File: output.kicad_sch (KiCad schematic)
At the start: 108 parts, among them J10 DB301V-3.5-3P-GN, J11 DB301V-3.5-3P-GN, J12 DB301V-3.5-3P-GN, J13 DB301V-3.5-3P-GN, J14 DB301V-3.5-3P-GN, J15 DB301V-3.5-3P-GN, J16 DB301V-3.5-3P-GN, J17 DB301V-3.5-3P-GN, J18 DB301V-3.5-3P-GN, J19 DB301V-3.5-3P-GN, J20 DB301V-3.5-3P-GN, J21 DB301V-3.5-3P-GN, J22 DB301V-3.5-3P-GN, J23 DB301V-3.5-3P-GN, J24 DB301V-3.5-3P-GN, J25 DB301V-3.5-3P-GN, J26 DB301V-3.5-3P-GN, J27 DB301V-3.5-3P-GN, J28 DB301V-3.5-3P-GN, J29 DB301V-3.5-3P-GN, J30 DB301V-3.5-3P-GN, J31 DB301V-3.5-3P-GN, J32 DB301V-3.5-3P-GN, J33 DB301V-3.5-3P-GN, J34 DB301V-3.5-3P-GN, J35 DB301V-3.5-3P-GN, J36 DB301V-3.5-3P-GN, J5 DB301V-3.5-3P-GN, J6 DB301V-3.5-3P-GN, J7 DB301V-3.5-3P-GN, J8 DB301V-3.5-3P-GN, J9 DB301V-3.5-3P-GN, U5 SN74LVC8T245PWR, U6 SN74LVC8T245PWR, U7 SN74LVC8T245PWR, U8 SN74LVC8T245PWR

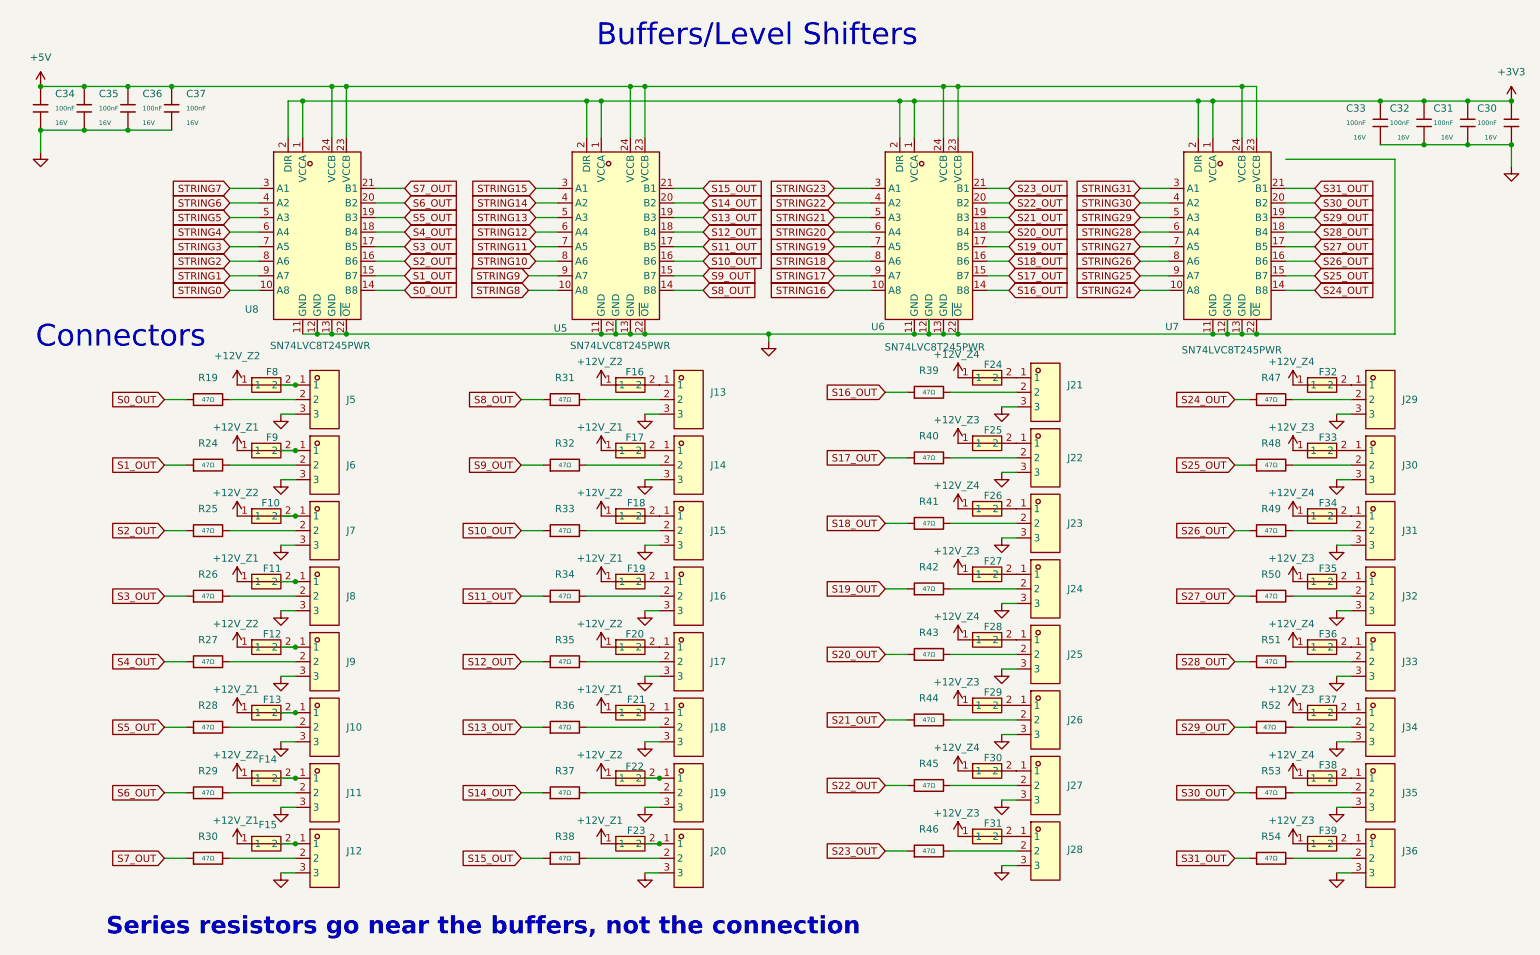
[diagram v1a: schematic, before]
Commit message: Zone silkscreen, 30V port PTCs, string renumbering
- Port PTCs: LUTE 1812L300/30GR (C48985875) imported via jlcimport, pins
  redrawn to match the old symbol; pads unchanged.
- Nets STRINGn/Sn_OUT renumbered by zone (Z1 S0-7 .. Z4 S24-31).
- Silkscreen: S<n>.Z<z> labels, + Zn - on input terminals, zone borders
  following the pours, zone key with voltage write-in, 5-24VDC/VIN labels.
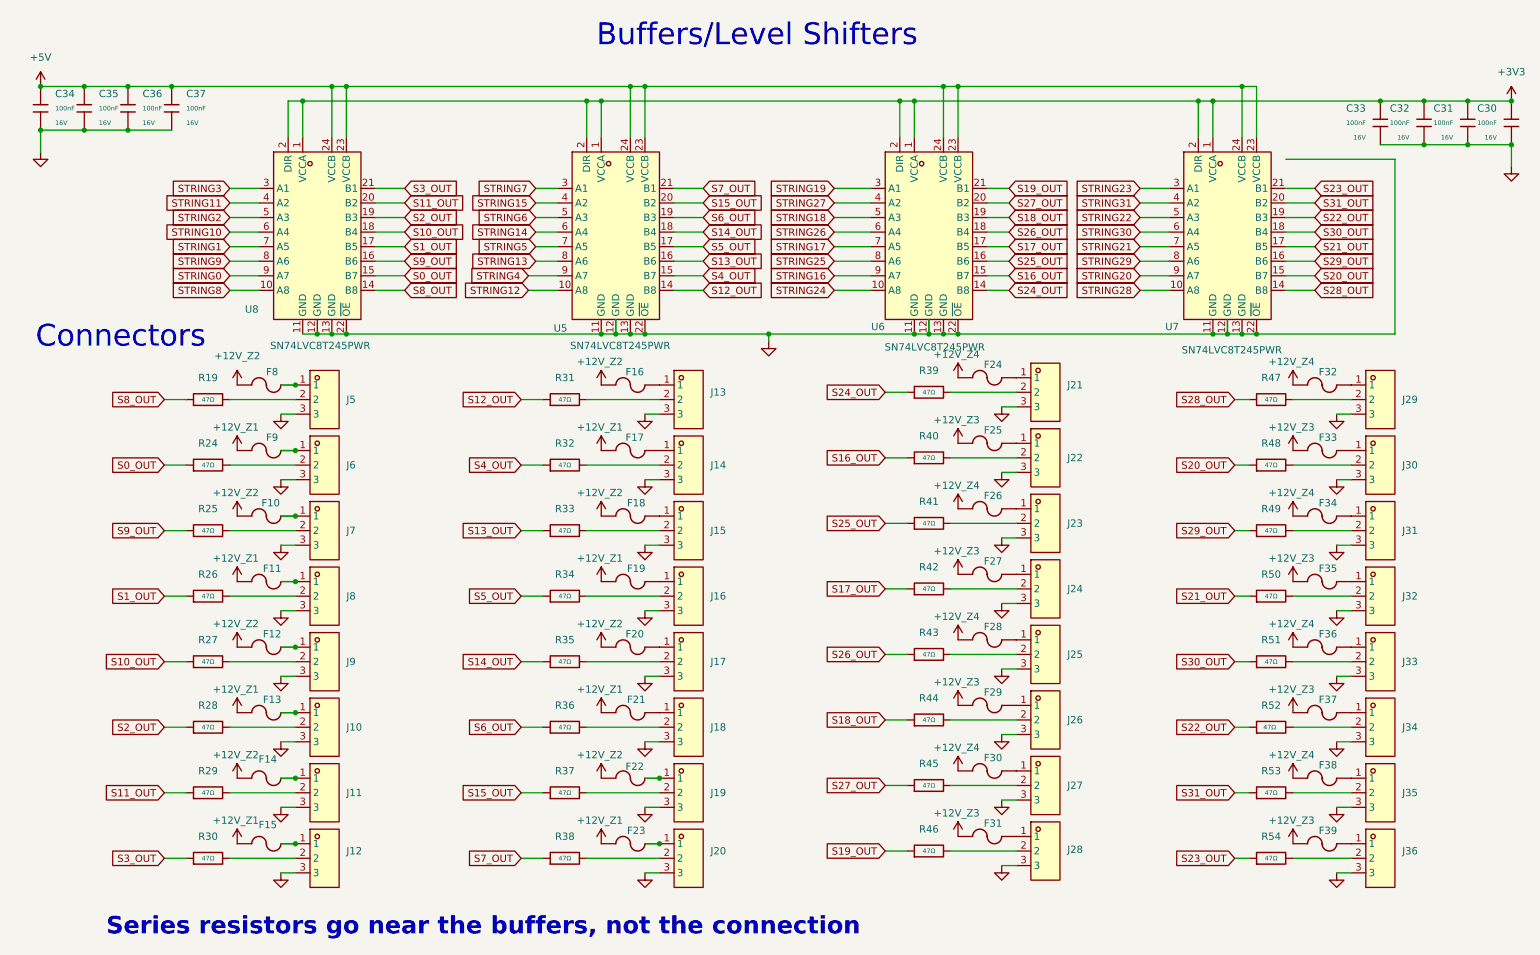
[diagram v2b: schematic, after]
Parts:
- F10, F11, F12, F13, F14, F15, F16, F17, F18, F19, F20, F21, F22, F23, F24, F25, F26, F27, F28, F29, F30, F31, F32, F33, F34, F35, F36, F37, F38, F39, F8, F9: value 1812L400/16GR -> 1812L300/30GR; footprint EasyEDA:F1812 -> JLCImport:1812L300_30GR; symbol EasyEDA:1812L400_16GR -> JLCImport:1812L300_30GR; LCSC (none) -> C48985875; LCSC Part C22374900 -> (none); Manufacturer (none) -> LUTE; Manufacturer Part (none) -> 1812L300/30GR
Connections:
- net S0_OUT: now also R24.1, U8.15 (B7); no longer R19.1, U8.14 (B8)
- net S10_OUT: now also R27.1, U8.18 (B4); no longer R33.1, U5.16 (B6)
- net S11_OUT: now also R29.1, U8.20 (B2); no longer R34.1, U5.17 (B5)
- net S12_OUT: now also R31.1, U5.14 (B8); no longer R35.1, U5.18 (B4)
- net S13_OUT: now also R33.1, U5.16 (B6); no longer R36.1, U5.19 (B3)
- net S14_OUT: now also R35.1, U5.18 (B4); no longer R37.1, U5.20 (B2)
- net S15_OUT: now also R37.1, U5.20 (B2); no longer R38.1, U5.21 (B1)
- net S16_OUT: now also R40.1, U6.15 (B7); no longer R39.1, U6.14 (B8)
- net S17_OUT: now also R42.1, U6.17 (B5); no longer R40.1, U6.15 (B7)
- net S18_OUT: now also R44.1, U6.19 (B3); no longer R41.1, U6.16 (B6)
- net S19_OUT: now also R46.1, U6.21 (B1); no longer R42.1, U6.17 (B5)
- net S1_OUT: now also R26.1, U8.17 (B5); no longer R24.1, U8.15 (B7)
- net S20_OUT: now also R48.1, U7.15 (B7); no longer R43.1, U6.18 (B4)
- net S21_OUT: now also R50.1, U7.17 (B5); no longer R44.1, U6.19 (B3)
- net S22_OUT: now also R52.1, U7.19 (B3); no longer R45.1, U6.20 (B2)
- net S23_OUT: now also R54.1, U7.21 (B1); no longer R46.1, U6.21 (B1)
- net S24_OUT: now also R39.1, U6.14 (B8); no longer R47.1, U7.14 (B8)
- net S25_OUT: now also R41.1, U6.16 (B6); no longer R48.1, U7.15 (B7)
- net S26_OUT: now also R43.1, U6.18 (B4); no longer R49.1, U7.16 (B6)
- net S27_OUT: now also R45.1, U6.20 (B2); no longer R50.1, U7.17 (B5)
- net S28_OUT: now also R47.1, U7.14 (B8); no longer R51.1, U7.18 (B4)
- net S29_OUT: now also R49.1, U7.16 (B6); no longer R52.1, U7.19 (B3)
- net S2_OUT: now also R28.1, U8.19 (B3); no longer R25.1, U8.16 (B6)
- net S30_OUT: now also R51.1, U7.18 (B4); no longer R53.1, U7.20 (B2)
- net S31_OUT: now also R53.1, U7.20 (B2); no longer R54.1, U7.21 (B1)
- net S3_OUT: now also R30.1, U8.21 (B1); no longer R26.1, U8.17 (B5)
- net S4_OUT: now also R32.1, U5.15 (B7); no longer R27.1, U8.18 (B4)
- net S5_OUT: now also R34.1, U5.17 (B5); no longer R28.1, U8.19 (B3)
- net S6_OUT: now also R36.1, U5.19 (B3); no longer R29.1, U8.20 (B2)
- net S7_OUT: now also R38.1, U5.21 (B1); no longer R30.1, U8.21 (B1)
- net S8_OUT: now also R19.1, U8.14 (B8); no longer R31.1, U5.14 (B8)
- net S9_OUT: now also R25.1, U8.16 (B6); no longer R32.1, U5.15 (B7)
- net STRING0: now also U8.9 (A7); no longer U8.10 (A8)
- net STRING1: now also U8.7 (A5); no longer U8.9 (A7)
- net STRING10: now also U8.6 (A4); no longer U5.8 (A6)
- net STRING11: now also U8.4 (A2); no longer U5.7 (A5)
- net STRING12: now also U5.10 (A8); no longer U5.6 (A4)
- net STRING13: now also U5.8 (A6); no longer U5.5 (A3)
- net STRING14: now also U5.6 (A4); no longer U5.4 (A2)
- net STRING15: now also U5.4 (A2); no longer U5.3 (A1)
- net STRING16: now also U6.9 (A7); no longer U6.10 (A8)
- net STRING17: now also U6.7 (A5); no longer U6.9 (A7)
- net STRING18: now also U6.5 (A3); no longer U6.8 (A6)
- net STRING19: now also U6.3 (A1); no longer U6.7 (A5)
- net STRING2: now also U8.5 (A3); no longer U8.8 (A6)
- net STRING20: now also U7.9 (A7); no longer U6.6 (A4)
- net STRING21: now also U7.7 (A5); no longer U6.5 (A3)
- net STRING22: now also U7.5 (A3); no longer U6.4 (A2)
- net STRING23: now also U7.3 (A1); no longer U6.3 (A1)
- net STRING24: now also U6.10 (A8); no longer U7.10 (A8)
- net STRING25: now also U6.8 (A6); no longer U7.9 (A7)
- net STRING26: now also U6.6 (A4); no longer U7.8 (A6)
- net STRING27: now also U6.4 (A2); no longer U7.7 (A5)
- net STRING28: now also U7.10 (A8); no longer U7.6 (A4)
- net STRING29: now also U7.8 (A6); no longer U7.5 (A3)
- net STRING3: now also U8.3 (A1); no longer U8.7 (A5)
- net STRING30: now also U7.6 (A4); no longer U7.4 (A2)
- net STRING31: now also U7.4 (A2); no longer U7.3 (A1)
- net STRING4: now also U5.9 (A7); no longer U8.6 (A4)
- net STRING5: now also U5.7 (A5); no longer U8.5 (A3)
- net STRING6: now also U5.5 (A3); no longer U8.4 (A2)
- net STRING7: now also U5.3 (A1); no longer U8.3 (A1)
- net STRING8: now also U8.10 (A8); no longer U5.10 (A8)
- net STRING9: now also U8.8 (A6); no longer U5.9 (A7)

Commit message: Rename 12V nets to VIN_SYS/VZ1-VZ4, update README for v5
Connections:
- net +12V_Z1 renamed VZ1
- net +12V_Z2 renamed VZ2
- net +12V_Z3 renamed VZ3
- net +12V_Z4 renamed VZ4
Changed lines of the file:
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@@
 			)
 		)
-		(property "Value" "+12V_Z4"
+		(property "Value" "VZ4"
 			(at 239.776 94.996 0)
 			(show_name no)
@@
 			)
 		)
-		(property "Value" "+12V_Z4"
+		(property "Value" "VZ4"
 			(at 239.776 117.856 0)
 			(show_name no)
@@
 			)
 		)
-		(property "Value" "+12V_Z2"
+		(property "Value" "VZ2"
 			(at 55.626 117.856 0)
 			(show_name no)
@@
 			)
 		)
-		(property "Value" "+12V_Z1"
+		(property "Value" "VZ1"
 			(at 119.126 129.286 0)
 			(show_name no)
@@
 			)
 		)
-		(property "Value" "+12V_Z3"
+		(property "Value" "VZ3"
 			(at 239.776 152.146 0)
 			(show_name no)
@@
 			)
 		)
-		(property "Value" "+12V_Z1"
+		(property "Value" "VZ1"
 			(at 55.626 152.146 0)
 			(show_name no)
@@
 			)
 		)
-		(property "Value" "+12V_Z4"
+		(property "Value" "VZ4"
 			(at 239.776 72.136 0)
 			(show_name no)
@@
 			)
 		)
-		(property "Value" "+12V_Z3"
+		(property "Value" "VZ3"
 			(at 181.356 82.296 0)
 			(show_name no)
@@
 			)
 		)
-		(property "Value" "+12V_Z1"
+		(property "Value" "VZ1"
 			(at 55.626 106.426 0)
 			(show_name no)
@@
 			)
 		)
-		(property "Value" "+12V_Z4"
+		(property "Value" "VZ4"
 			(at 181.356 93.726 0)
 			(show_name no)
@@
 			)
 		)
-		(property "Value" "+12V_Z1"
+		(property "Value" "VZ1"
 			(at 119.126 83.566 0)
 			(show_name no)
@@
 			)
 		)
-		(property "Value" "+12V_Z3"
+		(property "Value" "VZ3"
 			(at 239.776 129.286 0)
 			(show_name no)
@@
 			)
 		)
-		(property "Value" "+12V_Z2"
+		(property "Value" "VZ2"
 			(at 55.626 140.716 0)
 			(show_name no)
@@
 			)
 		)
-		(property "Value" "+12V_Z3"
+		(property "Value" "VZ3"
 			(at 181.356 150.876 0)
 			(show_name no)
@@
 			)
 		)
-		(property "Value" "+12V_Z2"
+		(property "Value" "VZ2"
 			(at 119.126 140.716 0)
 			(show_name no)
@@
 			)
 		)
-		(property "Value" "+12V_Z3"
+		(property "Value" "VZ3"
 			(at 239.776 83.566 0)
 			(show_name no)
@@
 			)
 		)
-		(property "Value" "+12V_Z4"
+		(property "Value" "VZ4"
 			(at 181.356 70.866 0)
 			(show_name no)
@@
 			)
 		)
-		(property "Value" "+12V_Z4"
+		(property "Value" "VZ4"
 			(at 181.356 139.446 0)
 			(show_name no)
@@
 			)
 		)
-		(property "Value" "+12V_Z3"
+		(property "Value" "VZ3"
 			(at 181.356 128.016 0)
 			(show_name no)
@@
 			)
 		)
-		(property "Value" "+12V_Z4"
+		(property "Value" "VZ4"
 			(at 181.356 116.586 0)
 			(show_name no)
@@
 			)
 		)
-		(property "Value" "+12V_Z3"
+		(property "Value" "VZ3"
 			(at 181.356 105.156 0)
 			(show_name no)
@@
 			)
 		)
-		(property "Value" "+12V_Z2"
+		(property "Value" "VZ2"
 			(at 55.88 71.12 0)
 			(show_name no)
@@
 			)
 		)
-		(property "Value" "+12V_Z1"
+		(property "Value" "VZ1"
 			(at 119.126 152.146 0)
 			(show_name no)
@@
 			)
 		)
-		(property "Value" "+12V_Z1"
+		(property "Value" "VZ1"
 			(at 55.626 129.286 0)
 			(show_name no)
@@
 			)
 		)
-		(property "Value" "+12V_Z2"
+		(property "Value" "VZ2"
 			(at 119.126 72.136 0)
 			(show_name no)
@@
 			)
 		)
-		(property "Value" "+12V_Z3"
+		(property "Value" "VZ3"
 			(at 239.776 106.426 0)
 			(show_name no)
@@
 			)
 		)
-		(property "Value" "+12V_Z1"
+		(property "Value" "VZ1"
 			(at 119.126 106.426 0)
 			(show_name no)
@@
 			)
 		)
-		(property "Value" "+12V_Z2"
+		(property "Value" "VZ2"
 			(at 119.126 117.856 0)
 			(show_name no)
@@
 			)
 		)
-		(property "Value" "+12V_Z2"
+		(property "Value" "VZ2"
 			(at 55.626 94.996 0)
 			(show_name no)
@@
 			)
 		)
-		(property "Value" "+12V_Z1"
+		(property "Value" "VZ1"
 			(at 55.626 83.566 0)
 			(show_name no)
@@
 			)
 		)
-		(property "Value" "+12V_Z4"
+		(property "Value" "VZ4"
 			(at 239.776 140.716 0)
 			(show_name no)
@@
 			)
 		)
-		(property "Value" "+12V_Z2"
+		(property "Value" "VZ2"
 			(at 119.126 94.996 0)
 			(show_name no)

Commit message: Data-line TVS on all 32 ports, Boot button beside the flash, audit doc
- D19-D50 SMF5.0A (C193402) from each port's data line (terminal side of
  the 47R) to GND, with a GND via at each anode.
- SW1/R1 moved beside U2: QSPI_SS loses its 109 mm B.Cu stub.
- docs/audit-v5.md: merged findings of the four design audits.
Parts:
- added D19, D20, D21, D22, D23, D24, D25, D26, D27, D28, D29, D30, D31, D32, D33, D34, D35, D36, D37, D38, D39, D40, D41, D42, D43, D44, D45, D46, D47, D48, D49, D50: SMF5.0A, JLCImport:SMF5_0A_C193402, symbol JLCImport:SMF5_0A_C193402
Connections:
- net GND: now also D19.2 (A), D20.2 (A), D21.2 (A), D22.2 (A), D23.2 (A), D24.2 (A), D25.2 (A), D26.2 (A), D27.2 (A), D28.2 (A), D29.2 (A), D30.2 (A), D31.2 (A), D32.2 (A), D33.2 (A), D34.2 (A), D35.2 (A), D36.2 (A), D37.2 (A), D38.2 (A), D39.2 (A), D40.2 (A), D41.2 (A), D42.2 (A), D43.2 (A), D44.2 (A), D45.2 (A), D46.2 (A), D47.2 (A), D48.2 (A), D49.2 (A), D50.2 (A)
- net at J22.2, R40.2: now also D36.1 (C)
- net at J11.2, R29.2: now also D25.1 (C)
- net at J35.2, R53.2: now also D49.1 (C)
- net at J26.2, R44.2: now also D40.1 (C)
- net at J12.2, R30.2: now also D26.1 (C)
- net at J34.2, R52.2: now also D48.1 (C)
- net at J20.2, R38.2: now also D34.1 (C)
- net at J9.2, R27.2: now also D23.1 (C)
- net at J18.2, R36.2: now also D32.1 (C)
- net at J15.2, R33.2: now also D29.1 (C)
- net at J33.2, R51.2: now also D47.1 (C)
- net at J36.2, R54.2: now also D50.1 (C)
- net at J27.2, R45.2: now also D41.1 (C)
- net at J8.2, R26.2: now also D22.1 (C)
- net at J31.2, R49.2: now also D45.1 (C)
- net at J28.2, R46.2: now also D42.1 (C)
- net at J32.2, R50.2: now also D46.1 (C)
- net at J5.2, R19.2: now also D19.1 (C)
- net at J19.2, R37.2: now also D33.1 (C)
- net at J7.2, R25.2: now also D21.1 (C)
- net at J24.2, R42.2: now also D38.1 (C)
- net at J13.2, R31.2: now also D27.1 (C)
- net at J16.2, R34.2: now also D30.1 (C)
- net at J14.2, R32.2: now also D28.1 (C)
- net at J29.2, R47.2: now also D43.1 (C)
- net at J30.2, R48.2: now also D44.1 (C)
- net at J21.2, R39.2: now also D35.1 (C)
- net at J25.2, R43.2: now also D39.1 (C)
- net at J23.2, R41.2: now also D37.1 (C)
- net at J10.2, R28.2: now also D24.1 (C)
- net at J6.2, R24.2: now also D20.1 (C)
- net at J17.2, R35.2: now also D31.1 (C)
